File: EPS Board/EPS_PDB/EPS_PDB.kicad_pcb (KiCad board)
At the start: 2 copper layers, 92 x 92 mm, 0 parts

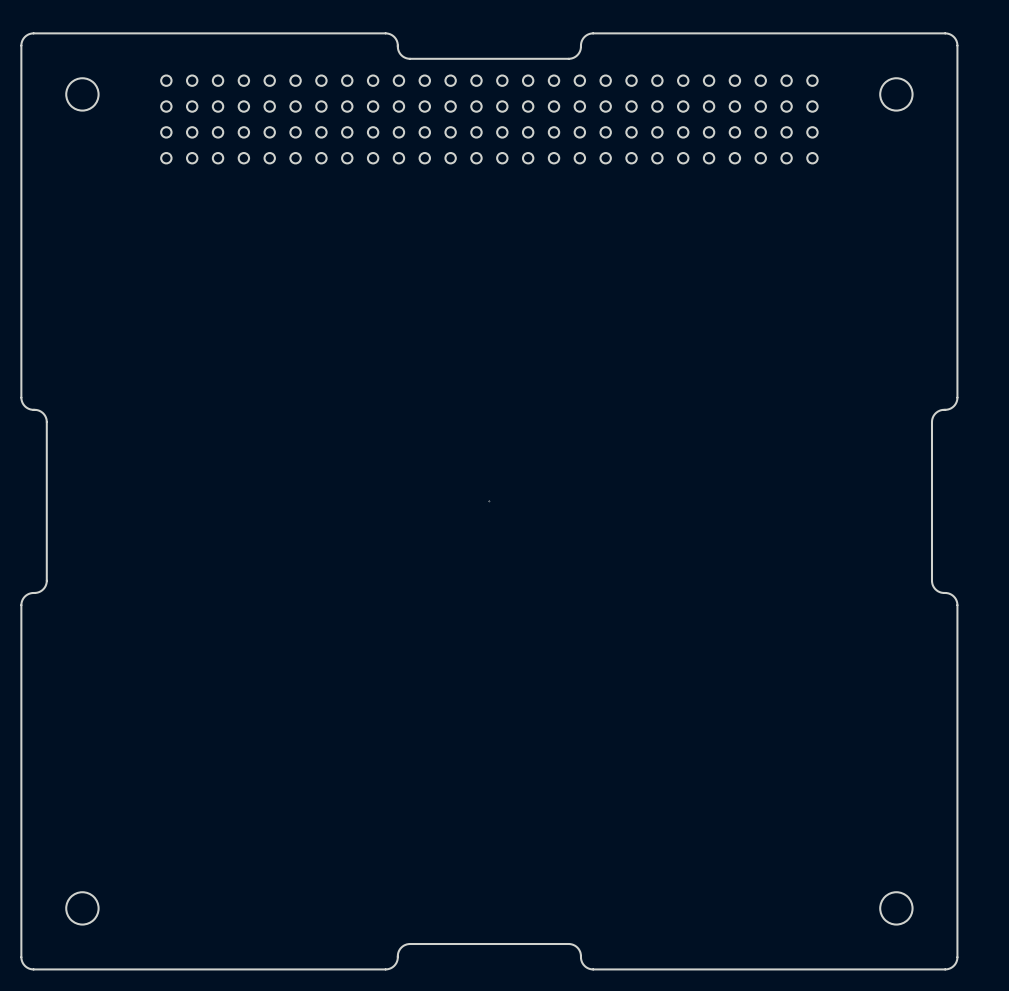
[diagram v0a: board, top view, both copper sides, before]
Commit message: Footprint assignment on EPS PDB Board
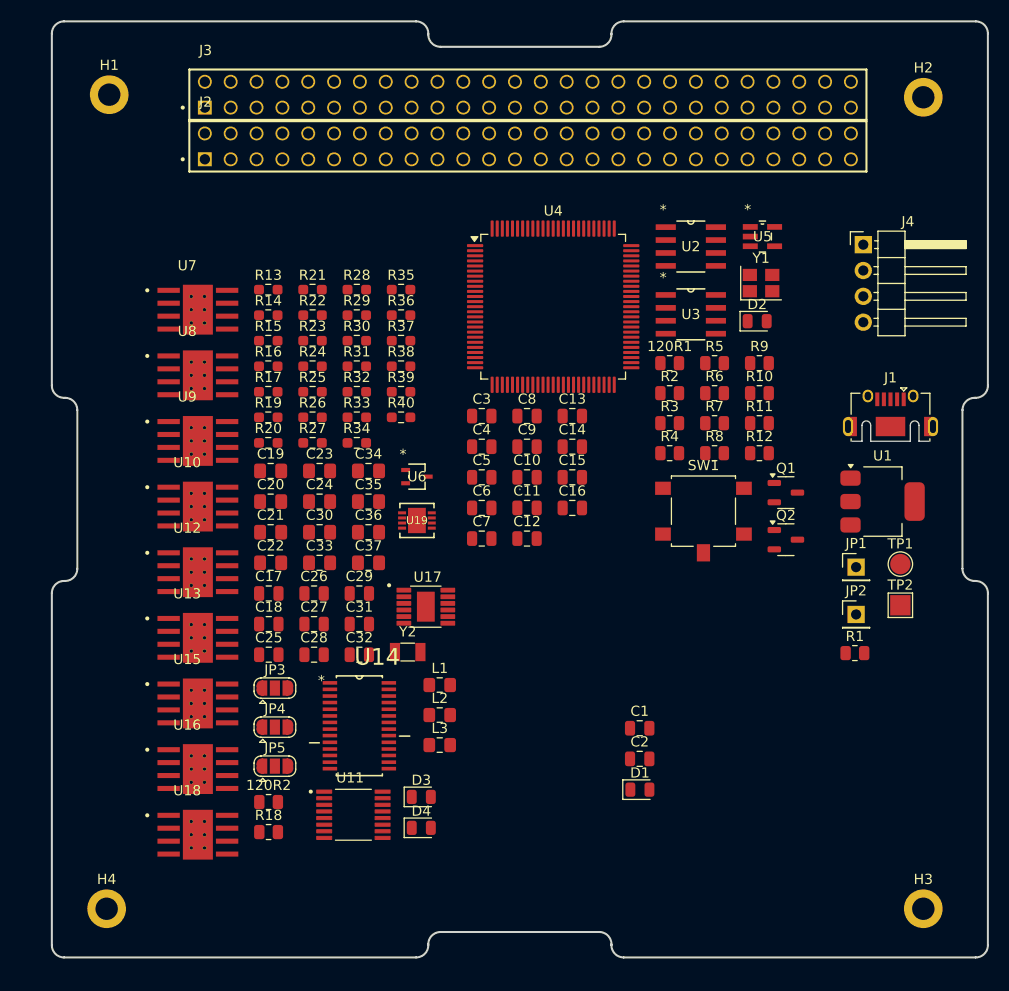
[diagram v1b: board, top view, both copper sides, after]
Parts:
- added 120R1: FerriteBead, Resistor_SMD:R_0805_2012Metric, F.Cu at (161.0, 78.7)
- added 120R2: FerriteBead, Resistor_SMD:R_0805_2012Metric, F.Cu at (121.6, 121.8)
- added C1: 22uF, Capacitor_SMD:C_0805_2012Metric, F.Cu at (158.1, 114.6)
- added C10: 100nF, Capacitor_SMD:C_0805_2012Metric, F.Cu at (147.0, 89.9)
- added C11: 10nF, Capacitor_SMD:C_0805_2012Metric, F.Cu at (147.0, 92.9)
- added C12: 1uF, Capacitor_SMD:C_0805_2012Metric, F.Cu at (147.0, 96.0)
- added C13: 1uF, Capacitor_SMD:C_0805_2012Metric, F.Cu at (151.4, 83.9)
- added C14: 100nF, Capacitor_SMD:C_0805_2012Metric, F.Cu at (151.4, 86.9)
- added C15: 10pF, Capacitor_SMD:C_0805_2012Metric, F.Cu at (151.4, 89.9)
- added C16: 10pF, Capacitor_SMD:C_0805_2012Metric, F.Cu at (151.4, 92.9)
- added C17: 10pF, Capacitor_SMD:C_0805_2012Metric, F.Cu at (121.6, 101.3)
- added C18: 10pF, Capacitor_SMD:C_0805_2012Metric, F.Cu at (121.6, 104.4)
- added C19: 0.47uF, Capacitor_SMD:C_0805_2012Metric_Pad1.18x1.45mm_HandSolder, F.Cu at (121.8, 89.3)
- added C2: 22uF, Capacitor_SMD:C_0805_2012Metric, F.Cu at (158.1, 117.6)
- added C20: 10uF, Capacitor_SMD:C_0805_2012Metric_Pad1.18x1.45mm_HandSolder, F.Cu at (121.8, 92.3)
- added C21: 10uF, Capacitor_SMD:C_0805_2012Metric_Pad1.18x1.45mm_HandSolder, F.Cu at (121.8, 95.3)
- added C22: TBD, Capacitor_SMD:C_0805_2012Metric_Pad1.18x1.45mm_HandSolder, F.Cu at (121.8, 98.3)
- added C23: TBD, Capacitor_SMD:C_0805_2012Metric_Pad1.18x1.45mm_HandSolder, F.Cu at (126.6, 89.3)
- added C24: TBD, Capacitor_SMD:C_0805_2012Metric_Pad1.18x1.45mm_HandSolder, F.Cu at (126.6, 92.3)
- added C25: 10uF, Capacitor_SMD:C_0805_2012Metric, F.Cu at (121.6, 107.4)
- added C26: C, Capacitor_SMD:C_0805_2012Metric, F.Cu at (126.0, 101.3)
- added C27: 10nF, Capacitor_SMD:C_0805_2012Metric, F.Cu at (126.0, 104.4)
- added C28: 1uF, Capacitor_SMD:C_0805_2012Metric, F.Cu at (126.0, 107.4)
- added C29: 1uF, Capacitor_SMD:C_0805_2012Metric, F.Cu at (130.5, 101.3)
- added C3: 10uF, Capacitor_SMD:C_0805_2012Metric, F.Cu at (142.5, 83.9)
- added C30: 4.7uF, Capacitor_SMD:C_0805_2012Metric_Pad1.18x1.45mm_HandSolder, F.Cu at (126.6, 95.3)
- added C31: 10uF, Capacitor_SMD:C_0805_2012Metric, F.Cu at (130.5, 104.4)
- added C32: C, Capacitor_SMD:C_0805_2012Metric, F.Cu at (130.5, 107.4)
- added C33: 2.2uF, Capacitor_SMD:C_0805_2012Metric_Pad1.18x1.45mm_HandSolder, F.Cu at (126.6, 98.3)
- added C34: 10uF, Capacitor_SMD:C_0805_2012Metric_Pad1.18x1.45mm_HandSolder, F.Cu at (131.4, 89.3)
- added C35: 47uF, Capacitor_SMD:C_0805_2012Metric_Pad1.18x1.45mm_HandSolder, F.Cu at (131.4, 92.3)
- added C36: 10uF, Capacitor_SMD:C_0805_2012Metric_Pad1.18x1.45mm_HandSolder, F.Cu at (131.4, 95.3)
- added C37: 2.2uF, Capacitor_SMD:C_0805_2012Metric_Pad1.18x1.45mm_HandSolder, F.Cu at (131.4, 98.3)
- added C4: 100nF, Capacitor_SMD:C_0805_2012Metric, F.Cu at (142.5, 86.9)
- added C5: 100nF, Capacitor_SMD:C_0805_2012Metric, F.Cu at (142.5, 89.9)
- added C6: 100nF, Capacitor_SMD:C_0805_2012Metric, F.Cu at (142.5, 92.9)
- added C7: 100nF, Capacitor_SMD:C_0805_2012Metric, F.Cu at (142.5, 96.0)
- added C8: 100nF, Capacitor_SMD:C_0805_2012Metric, F.Cu at (147.0, 83.9)
- added C9: 100nF, Capacitor_SMD:C_0805_2012Metric, F.Cu at (147.0, 86.9)
- added D1: POWER_LED, LED_SMD:LED_0805_2012Metric, F.Cu at (158.1, 120.6)
- added D2: EPS_LED, LED_SMD:LED_0805_2012Metric, F.Cu at (169.6, 74.6)
- added D3: D_Schottky, Diode_SMD:D_0805_2012Metric, F.Cu at (136.6, 121.3)
- added D4: D, Diode_SMD:D_0805_2012Metric, F.Cu at (136.6, 124.4)
- added H1: MountingHole_Pad, MountingHole:MountingHole_2.2mm_M2_DIN965_Pad, F.Cu at (105.9, 52.3)
- added H2: MountingHole_Pad, MountingHole:MountingHole_2.2mm_M2_DIN965_Pad, F.Cu at (185.9, 52.6)
- added H3: MountingHole_Pad, MountingHole:MountingHole_2.2mm_M2_DIN965_Pad, F.Cu at (185.9, 132.3)
- added H4: MountingHole_Pad, MountingHole:MountingHole_2.2mm_M2_DIN965_Pad, F.Cu at (105.7, 132.3)
- added J1: USB_B_Micro, Connector_USB:USB_Micro-AB_Molex_47590-0001, F.Cu at (182.7, 84.9)
- added J2: Conn_02x26_Odd_Even, PC104_BUS:SAMTEC_ESQ-126-39-G-D, F.Cu at (178.2, 58.7)
- added J3: Conn_02x26_Odd_Even, PC104_BUS:SAMTEC_ESQ-126-39-G-D, F.Cu at (178.2, 53.6)
- added J4: Conn_01x04_Pin, Connector_PinHeader_2.54mm:PinHeader_1x04_P2.54mm_Horizontal, F.Cu at (180.0, 67.1)
- added JP1: USB_POW_EN, Connector_PinHeader_2.54mm:PinHeader_1x01_P2.54mm_Vertical, F.Cu at (179.3, 98.8)
- added JP2: Jumper_2_Bridged, Connector_PinHeader_2.54mm:PinHeader_1x01_P2.54mm_Vertical, F.Cu at (179.3, 103.4)
- added JP3: ~, Jumper:SolderJumper-3_P1.3mm_Open_RoundedPad1.0x1.5mm, F.Cu at (122.2, 110.6)
- added JP4: Jumper_3_Bridged12, Jumper:SolderJumper-3_P1.3mm_Open_RoundedPad1.0x1.5mm, F.Cu at (122.2, 114.5)
- added JP5: ~, Jumper:SolderJumper-3_P1.3mm_Open_RoundedPad1.0x1.5mm, F.Cu at (122.2, 118.3)
- added L1: 16uH, Inductor_SMD:L_0805_2012Metric_Pad1.15x1.40mm_HandSolder, F.Cu at (138.4, 110.3)
- added L2: 16uH, Inductor_SMD:L_0805_2012Metric_Pad1.15x1.40mm_HandSolder, F.Cu at (138.4, 113.3)
- added L3: 1.3uH, Inductor_SMD:L_0805_2012Metric_Pad1.15x1.40mm_HandSolder, F.Cu at (138.4, 116.2)
- added Q1: PMOS, Package_TO_SOT_SMD:SOT-23-3, F.Cu at (172.4, 91.4)
- added Q2: PMOS, Package_TO_SOT_SMD:SOT-23-3, F.Cu at (172.4, 96.1)
- added R1: 1k5, Resistor_SMD:R_0805_2012Metric, F.Cu at (179.2, 107.2)
- added R10: 1k5, Resistor_SMD:R_0805_2012Metric, F.Cu at (169.8, 81.7)
- added R11: 1k5, Resistor_SMD:R_0805_2012Metric, F.Cu at (169.8, 84.6)
- added R12: 0, Resistor_SMD:R_0805_2012Metric, F.Cu at (169.8, 87.6)
- added R13: 10k, Resistor_SMD:R_0603_1608Metric_Pad0.98x0.95mm_HandSolder, F.Cu at (121.5, 71.5)
- added R14: 10k, Resistor_SMD:R_0603_1608Metric_Pad0.98x0.95mm_HandSolder, F.Cu at (121.5, 74.0)
- added R15: 10k, Resistor_SMD:R_0603_1608Metric_Pad0.98x0.95mm_HandSolder, F.Cu at (121.5, 76.5)
- added R16: 10k, Resistor_SMD:R_0603_1608Metric_Pad0.98x0.95mm_HandSolder, F.Cu at (121.5, 79.0)
- added R17: 10k, Resistor_SMD:R_0603_1608Metric_Pad0.98x0.95mm_HandSolder, F.Cu at (121.5, 81.5)
- added R18: 130k, Resistor_SMD:R_0805_2012Metric, F.Cu at (121.6, 124.8)
- added R19: 10k, Resistor_SMD:R_0603_1608Metric_Pad0.98x0.95mm_HandSolder, F.Cu at (121.5, 84.0)
- added R2: R, Resistor_SMD:R_0805_2012Metric, F.Cu at (161.0, 81.7)
- added R20: 10k, Resistor_SMD:R_0603_1608Metric_Pad0.98x0.95mm_HandSolder, F.Cu at (121.5, 86.5)
- added R21: 2.2k, Resistor_SMD:R_0603_1608Metric_Pad0.98x0.95mm_HandSolder, F.Cu at (125.9, 71.5)
- added R22: 10k, Resistor_SMD:R_0603_1608Metric_Pad0.98x0.95mm_HandSolder, F.Cu at (125.9, 74.0)
- added R23: 10k, Resistor_SMD:R_0603_1608Metric_Pad0.98x0.95mm_HandSolder, F.Cu at (125.9, 76.5)
- added R24: 10k, Resistor_SMD:R_0603_1608Metric_Pad0.98x0.95mm_HandSolder, F.Cu at (125.9, 79.0)
- added R25: 10, Resistor_SMD:R_0603_1608Metric_Pad0.98x0.95mm_HandSolder, F.Cu at (125.9, 81.5)
- added R26: 400k, Resistor_SMD:R_0603_1608Metric_Pad0.98x0.95mm_HandSolder, F.Cu at (125.9, 84.0)
- added R27: 2.2k, Resistor_SMD:R_0603_1608Metric_Pad0.98x0.95mm_HandSolder, F.Cu at (125.9, 86.5)
- added R28: 510, Resistor_SMD:R_0603_1608Metric_Pad0.98x0.95mm_HandSolder, F.Cu at (130.2, 71.5)
- added R29: 130k, Resistor_SMD:R_0603_1608Metric_Pad0.98x0.95mm_HandSolder, F.Cu at (130.2, 74.0)
- added R3: R, Resistor_SMD:R_0805_2012Metric, F.Cu at (161.0, 84.6)
- added R30: TBD, Resistor_SMD:R_0603_1608Metric_Pad0.98x0.95mm_HandSolder, F.Cu at (130.2, 76.5)
- added R31: 15k, Resistor_SMD:R_0603_1608Metric_Pad0.98x0.95mm_HandSolder, F.Cu at (130.2, 79.0)
- added R32: 400k, Resistor_SMD:R_0603_1608Metric_Pad0.98x0.95mm_HandSolder, F.Cu at (130.2, 81.5)
- added R33: 400k, Resistor_SMD:R_0603_1608Metric_Pad0.98x0.95mm_HandSolder, F.Cu at (130.2, 84.0)
- added R34: 560, Resistor_SMD:R_0603_1608Metric_Pad0.98x0.95mm_HandSolder, F.Cu at (130.2, 86.5)
- added R35: 1.3k, Resistor_SMD:R_0603_1608Metric_Pad0.98x0.95mm_HandSolder, F.Cu at (134.6, 71.5)
- added R36: 400k, Resistor_SMD:R_0603_1608Metric_Pad0.98x0.95mm_HandSolder, F.Cu at (134.6, 74.0)
- added R37: 400k, Resistor_SMD:R_0603_1608Metric_Pad0.98x0.95mm_HandSolder, F.Cu at (134.6, 76.5)
- added R38: 560, Resistor_SMD:R_0603_1608Metric_Pad0.98x0.95mm_HandSolder, F.Cu at (134.6, 79.0)
- added R39: 1.3k, Resistor_SMD:R_0603_1608Metric_Pad0.98x0.95mm_HandSolder, F.Cu at (134.6, 81.5)
- added R4: 10k, Resistor_SMD:R_0805_2012Metric, F.Cu at (161.0, 87.6)
- added R40: 560, Resistor_SMD:R_0603_1608Metric_Pad0.98x0.95mm_HandSolder, F.Cu at (134.6, 84.0)
- added R5: R, Resistor_SMD:R_0805_2012Metric, F.Cu at (165.4, 78.7)
- added R6: R, Resistor_SMD:R_0805_2012Metric, F.Cu at (165.4, 81.7)
- added R7: 1k5, Resistor_SMD:R_0805_2012Metric, F.Cu at (165.4, 84.6)
- added R8: 1k5, Resistor_SMD:R_0805_2012Metric, F.Cu at (165.4, 87.6)
- added R9: 1k5, Resistor_SMD:R_0805_2012Metric, F.Cu at (169.8, 78.7)
- added SW1: SW_SPDT, Button_Switch_SMD:SW_SPST_B3S-1100, F.Cu at (164.3, 94.2)
- added TP1: TestPoint, TestPoint:TestPoint_Pad_D2.0mm, F.Cu at (183.7, 98.5)
- added TP2: TestPoint, TestPoint:TestPoint_Pad_2.0x2.0mm, F.Cu at (183.7, 102.5)
- added U1: AMS1117-3.3, Package_TO_SOT_SMD:SOT-223-3_TabPin2, F.Cu at (181.9, 92.3)
- added U10: TPS259621DDAT, TPS259621DDAT:IC_TPS259621DDAT, F.Cu at (114.6, 92.8)
- added U11: LM5000-3MTCX, LM500:SOP65P640X120-16N, F.Cu at (129.9, 123.1)
- added U12: TPS259621DDAT, TPS259621DDAT:IC_TPS259621DDAT, F.Cu at (114.6, 99.3)
- added U13: TPS259621DDAT, TPS259621DDAT:IC_TPS259621DDAT, F.Cu at (114.6, 105.7)
- added U14: AD7708BRUZ, AD7708BRUZ:SOP65P638X110-28N, F.Cu at (130.5, 114.3)
- added U15: TPS259621DDAT, TPS259621DDAT:IC_TPS259621DDAT, F.Cu at (114.6, 112.2)
- added U16: TPS259621DDAT, TPS259621DDAT:IC_TPS259621DDAT, F.Cu at (114.6, 118.6)
- added U17: LTC3624EMSE-3.3PBF, LTC3624EMSE-3.3PBF:SOP65P490X110-13N, F.Cu at (137.0, 102.6)
- added U18: TPS259621DDAT, TPS259621DDAT:IC_TPS259621DDAT, F.Cu at (114.6, 125.1)
- added U19: LTC3624IDD-25PBF, LTC3624IDD-25PBF:DFN-8_DD, F.Cu at (136.2, 94.2)
- added U2: SN65HVD256D, SN65HVD256D:D8, F.Cu at (163.1, 67.2)
- added U3: SN65HVD256D, SN65HVD256D:D8, F.Cu at (163.1, 73.9)
- added U4: STM32L476VET6, Package_QFP:LQFP-100_14x14mm_P0.5mm, F.Cu at (149.6, 73.2)
- added U5: TPS3824-33QDBVRQ1, TPS3824:tps3824, F.Cu at (170.1, 66.3)
- added U6: TS4061BICT-1.25, TS4061BICT:SOT323-3L_1P35X2P2X0P65_STM, F.Cu at (136.2, 89.9)
- added U7: TPS259621DDAT, TPS259621DDAT:IC_TPS259621DDAT, F.Cu at (114.6, 73.5)
- added U8: TPS259621DDAT, TPS259621DDAT:IC_TPS259621DDAT, F.Cu at (114.6, 79.9)
- added U9: TPS259621DDAT, TPS259621DDAT:IC_TPS259621DDAT, F.Cu at (114.6, 86.4)
- added Y1: 32MHz, Crystal:Crystal_SMD_Abracon_ABM8AIG-4Pin_3.2x2.5mm, F.Cu at (170.0, 70.8)
- added Y2: 32.768kHz, Crystal:Crystal_SMD_3215-2Pin_3.2x1.5mm, F.Cu at (135.2, 107.1)
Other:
- outline, holes or cut-outs redrawn

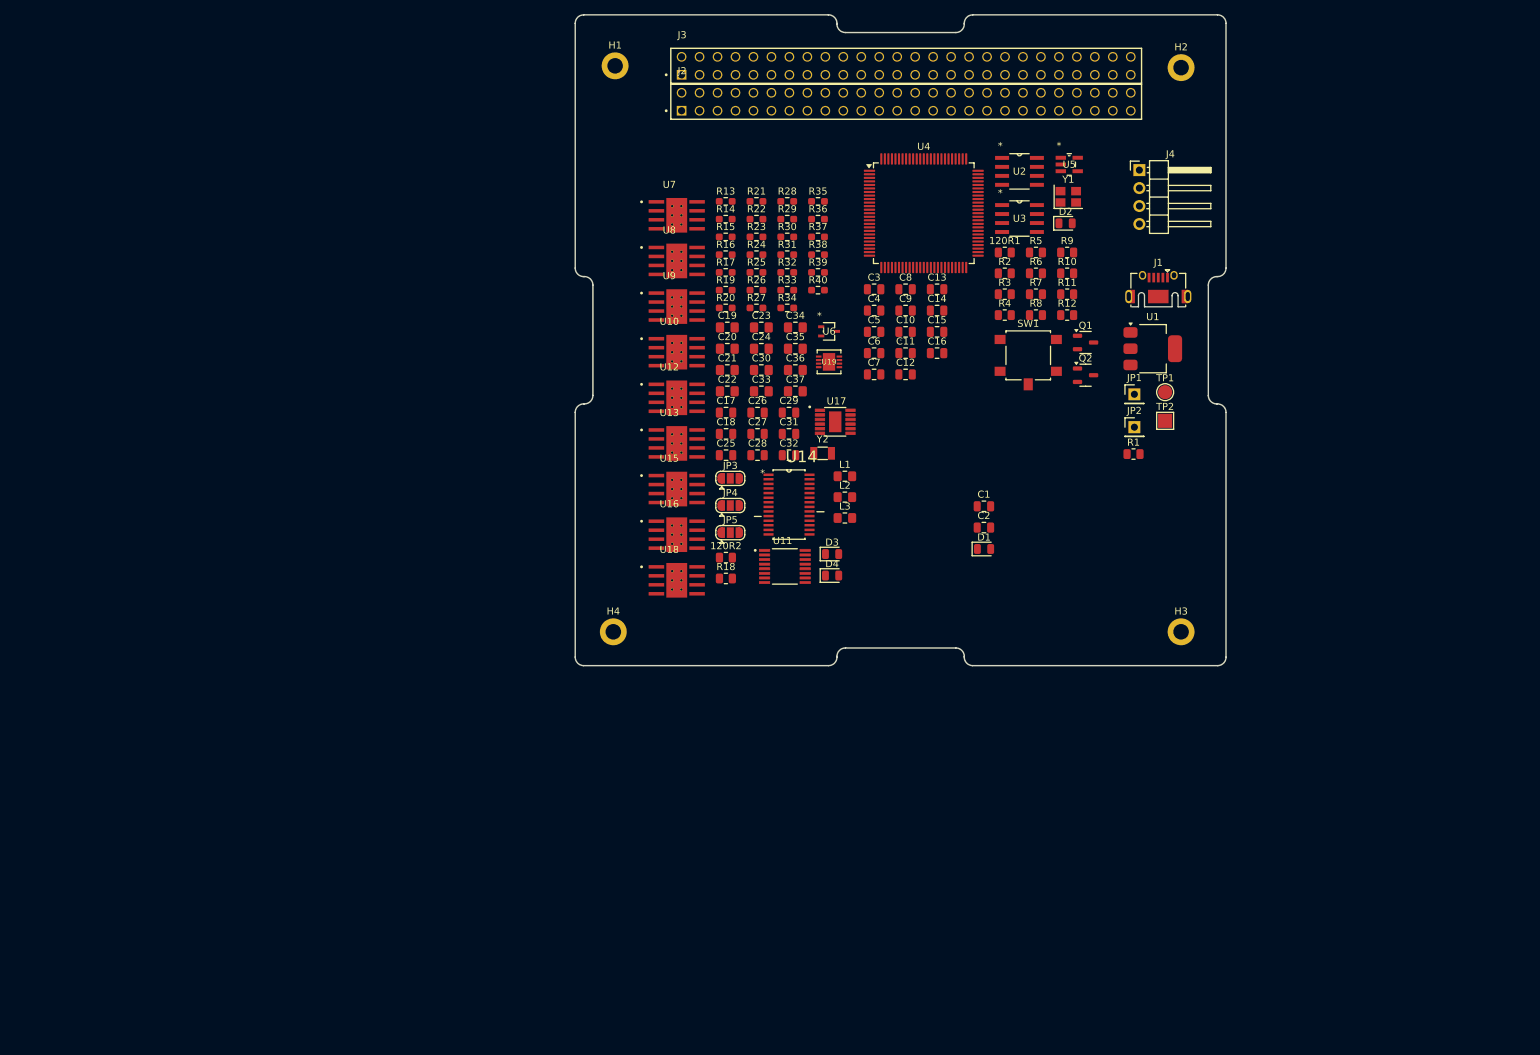
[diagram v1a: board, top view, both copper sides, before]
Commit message: Started EPS PDB PCB Layout
Modified footprint of PC104 Bus
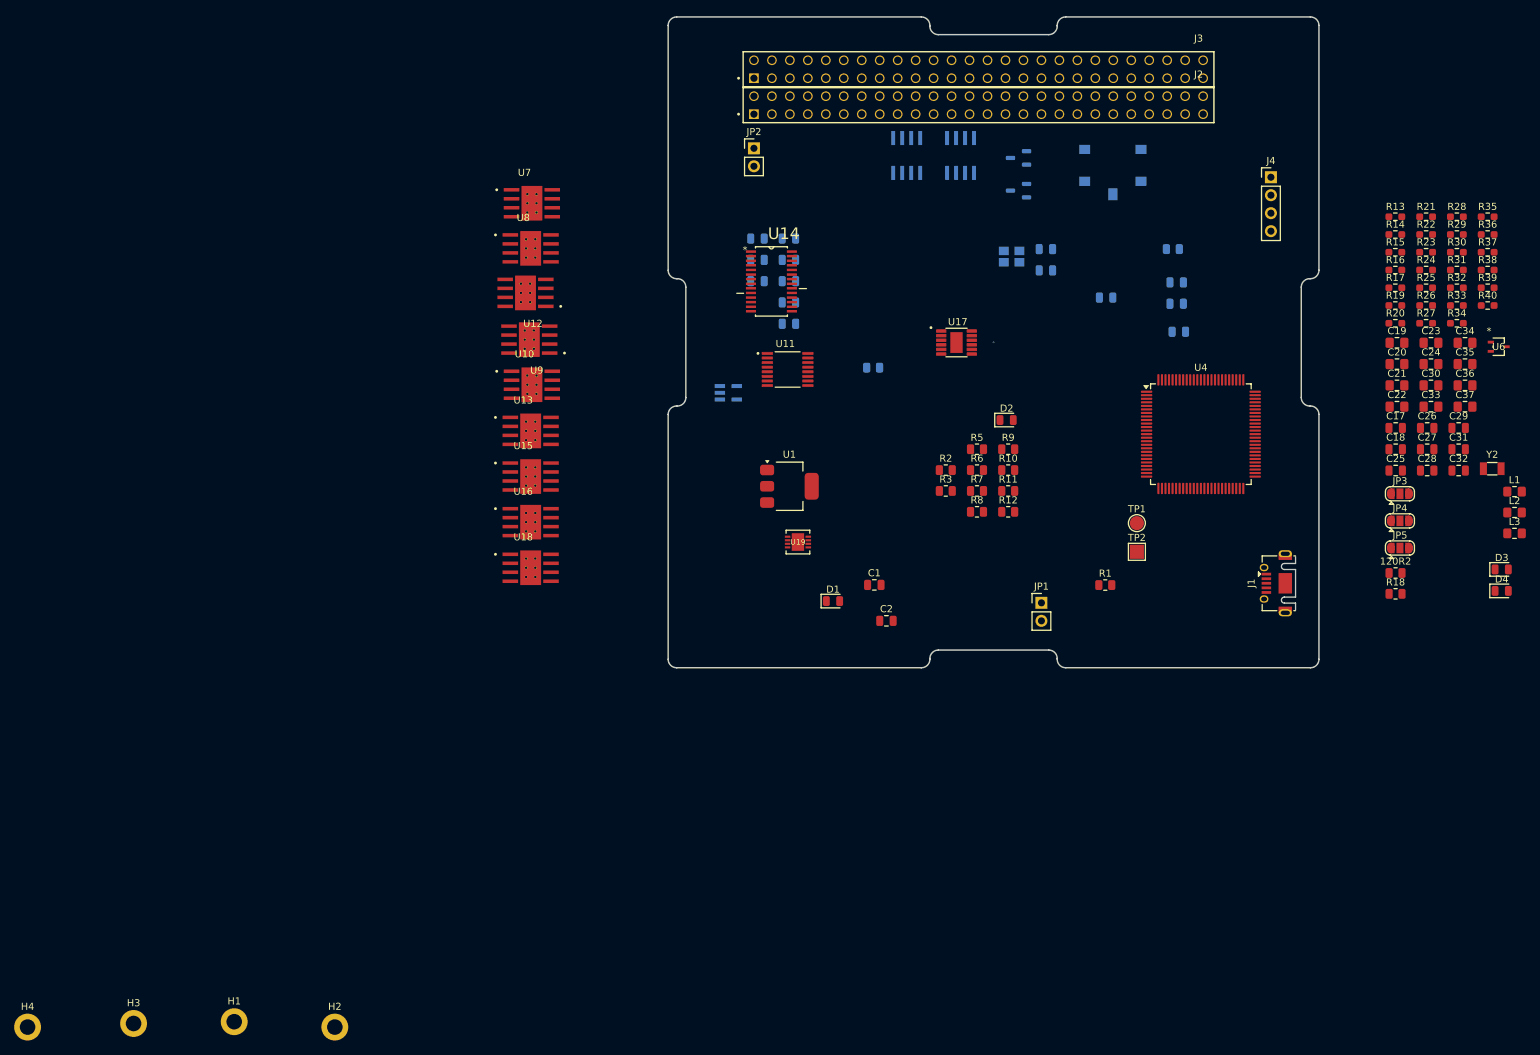
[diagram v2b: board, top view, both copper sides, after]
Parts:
- 120R1, C10, C11, C12, C13, C14, C15, C16, C3, C4, C5, C6, C7, C8, C9, Q1, Q2, R4, SW1, U2, U3, U5, Y1: moved to B.Cu
- J4: footprint Connector_PinHeader_2.54mm:PinHeader_1x04_P2.54mm_Horizontal -> Connector_PinHeader_2.54mm:PinHeader_1x04_P2.54mm_Vertical
- JP1, JP2: footprint Connector_PinHeader_2.54mm:PinHeader_1x01_P2.54mm_Vertical -> Connector_PinHeader_2.54mm:PinHeader_1x02_P2.54mm_Vertical
- moved H2 180.9 mm to (66.3, 188.2)
- moved H3 158.1 mm to (37.8, 187.7)
- moved H1 145.5 mm to (52.1, 187.5)
- moved H4 99.9 mm to (22.9, 188.2)
- moved C17 94.7 mm to (216.3, 103.5)
- moved C18 94.7 mm to (216.3, 106.5)
- moved C19 94.7 mm to (216.4, 91.5)
- moved C20 94.7 mm to (216.4, 94.5)
- moved C21 94.7 mm to (216.4, 97.5)
- moved C22 94.7 mm to (216.4, 100.5)
- moved C23 94.7 mm to (221.3, 91.5)
- moved C24 94.7 mm to (221.3, 94.5)
- moved C25 94.7 mm to (216.3, 109.5)
- moved C29 94.7 mm to (225.2, 103.5)
- moved C30 94.7 mm to (221.3, 97.5)
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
